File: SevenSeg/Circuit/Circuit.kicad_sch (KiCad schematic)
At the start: 13 parts, among them K1 ATmega328P-P, K1 BC337, K2 BC337, K3 BC337, K4 BC337, K5 BC337, P1 5161AS, P2 5641AS

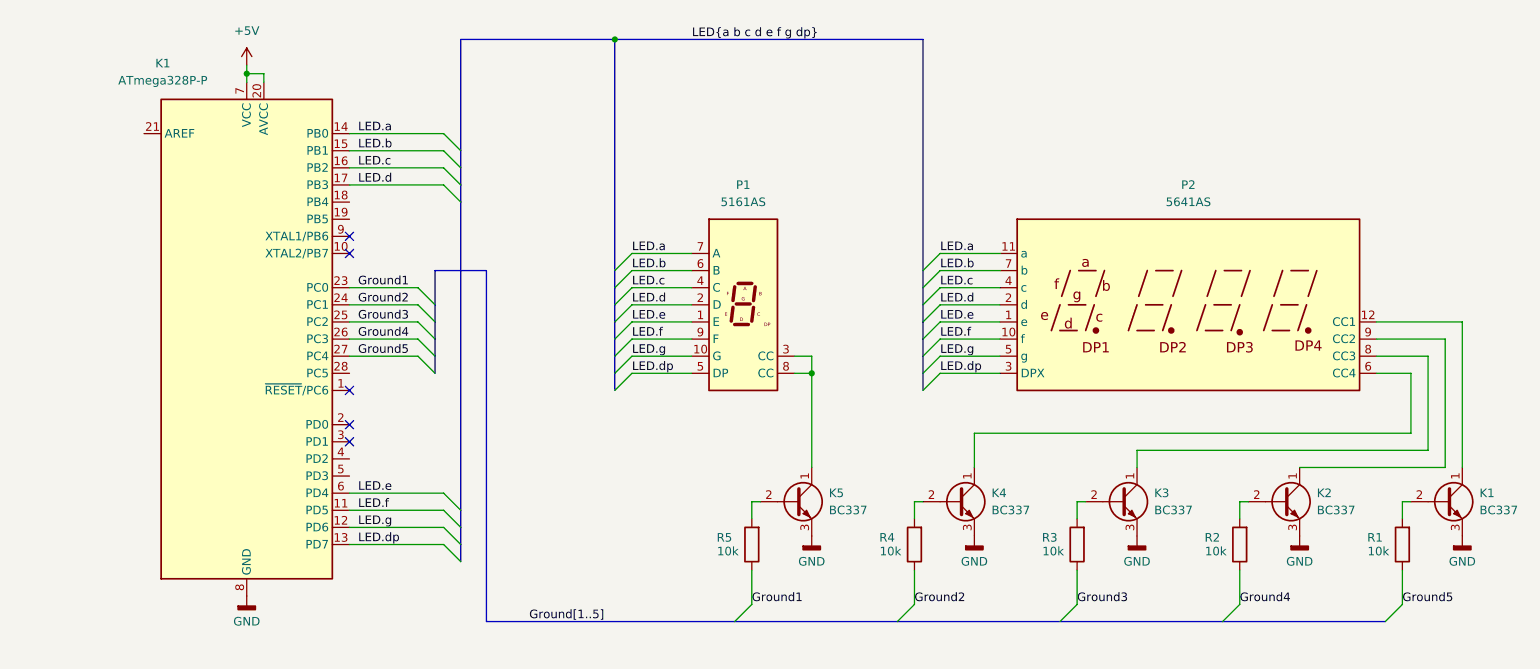
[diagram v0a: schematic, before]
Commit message: Fixed timing bug
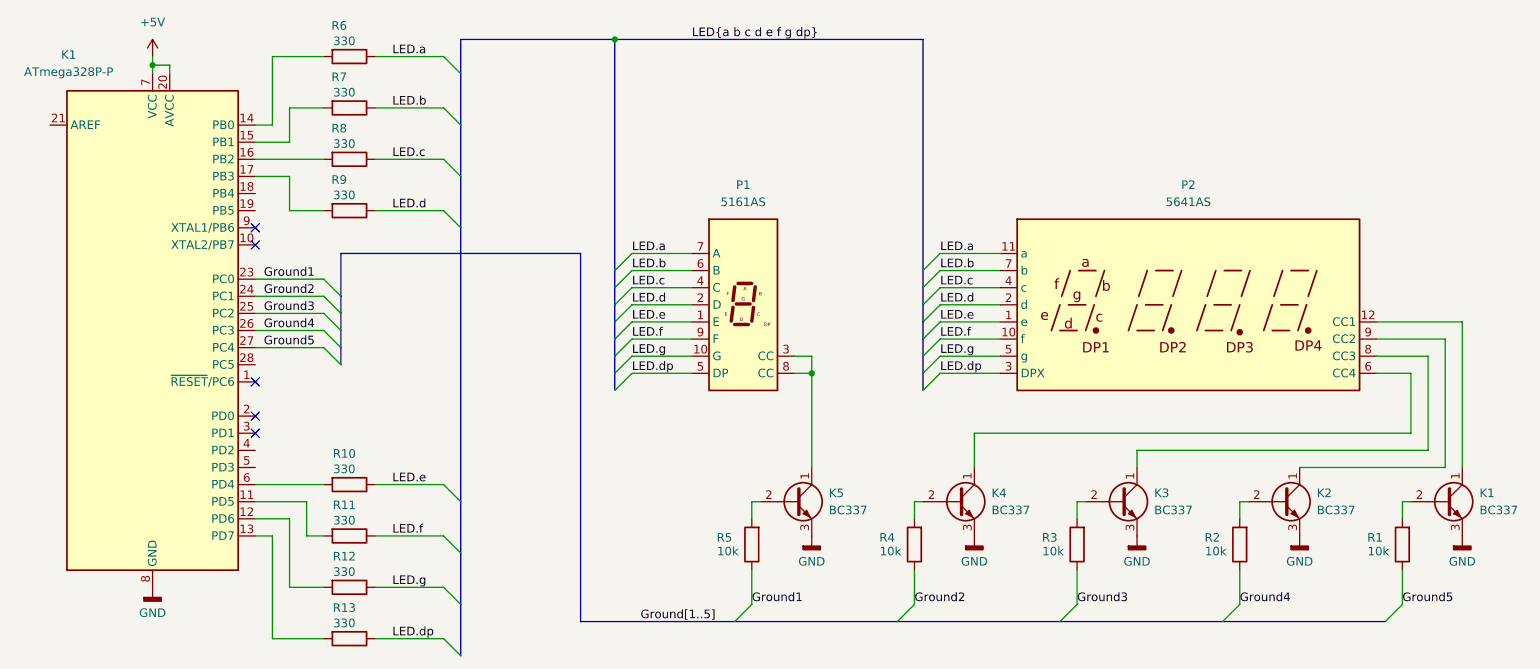
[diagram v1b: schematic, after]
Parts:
- added R10, R11, R12, R13, R6, R7, R8, R9: 330, symbol Device:R
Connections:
- net LED.a: now also R6.1; no longer K1.14 (PB0)
- net LED.b: now also R7.1; no longer K1.15 (PB1)
- net LED.c: now also R8.1; no longer K1.16 (PB2)
- net LED.d: now also R9.1; no longer K1.17 (PB3)
- net LED.dp: now also R13.1; no longer K1.13 (PD7)
- net LED.e: now also R10.1; no longer K1.6 (PD4)
- net LED.f: now also R11.1; no longer K1.11 (PD5)
- net LED.g: now also R12.1; no longer K1.12 (PD6)
- new net: K1.15 (PB1), R7.2
- new net: K1.12 (PD6), R12.2
- new net: K1.17 (PB3), R9.2
- new net: K1.14 (PB0), R6.2
- new net: K1.6 (PD4), R10.2
- new net: K1.13 (PD7), R13.2
- new net: K1.11 (PD5), R11.2
- new net: K1.16 (PB2), R8.2
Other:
- moved on the sheet: K1

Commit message: Updated Plan
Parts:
- added P3: Rot, symbol Device:LED
- added R14: 330, symbol Device:R
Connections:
- net GND: now also P3.1 (K)
- net at K1.28 (PC5): now also R14.2
- new net: P3.2 (A), R14.1
